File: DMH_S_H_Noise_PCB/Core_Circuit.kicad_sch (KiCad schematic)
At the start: 63 parts, among them Q1 BC548, Q2 MMBFJ113, Q3 BC548, SW1 SW_Push, SW2 SW_SPDT_321, U1 TL074, U2 TL072, U3 TL074

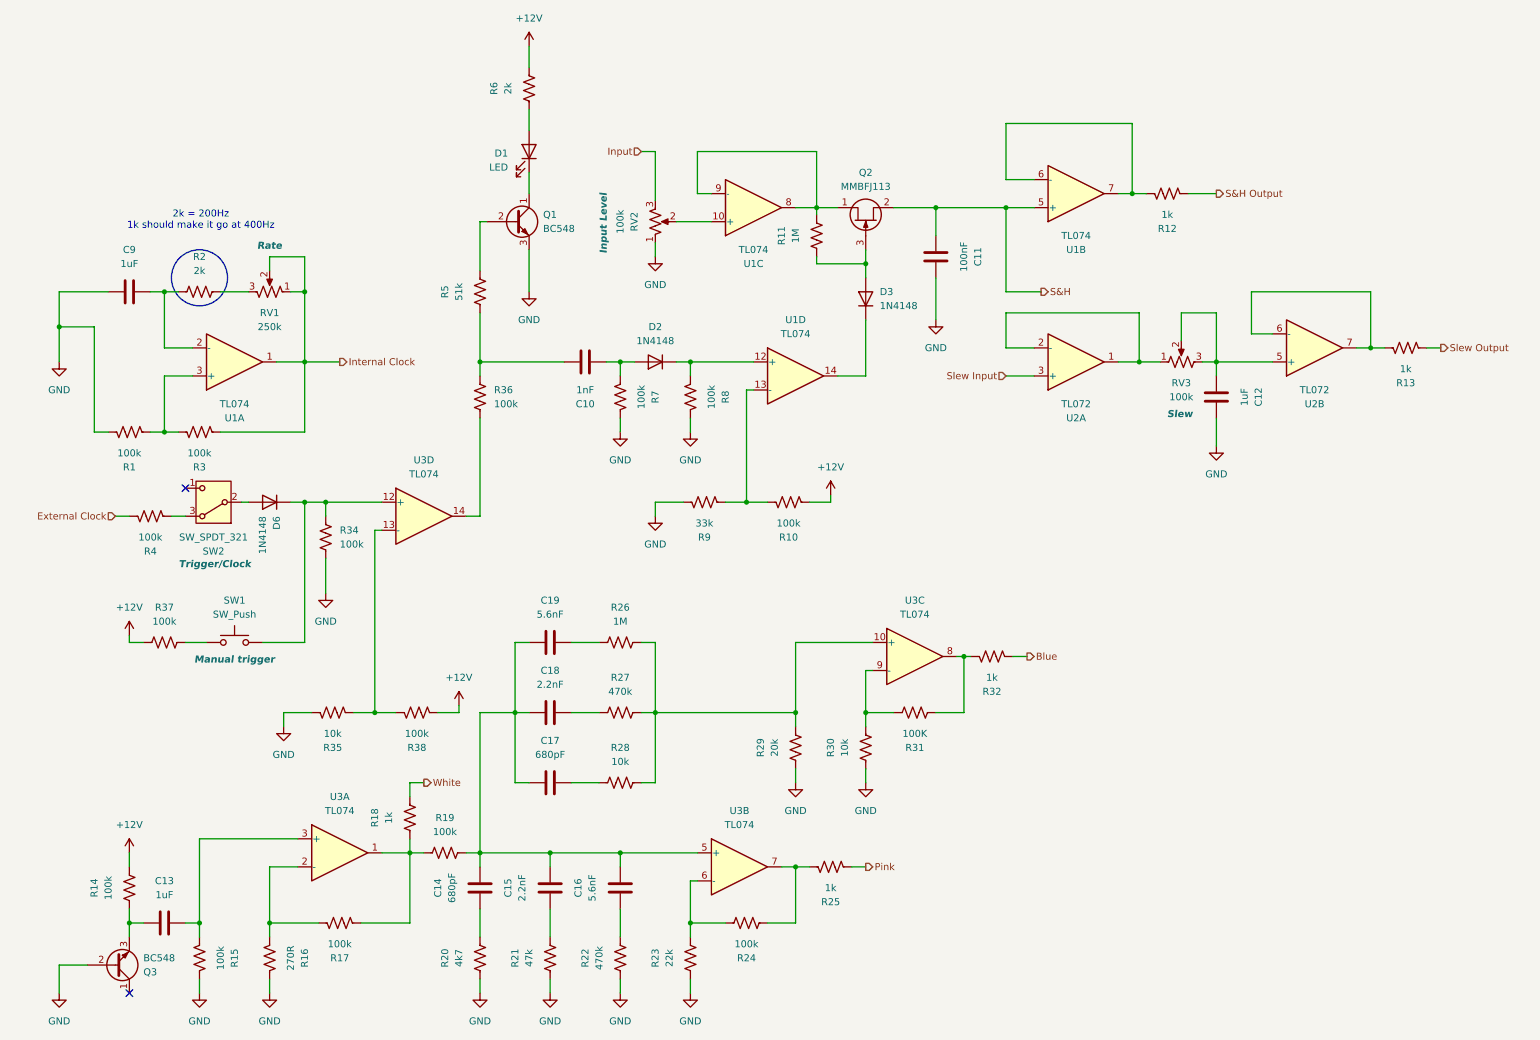
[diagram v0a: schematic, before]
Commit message: Added clock output
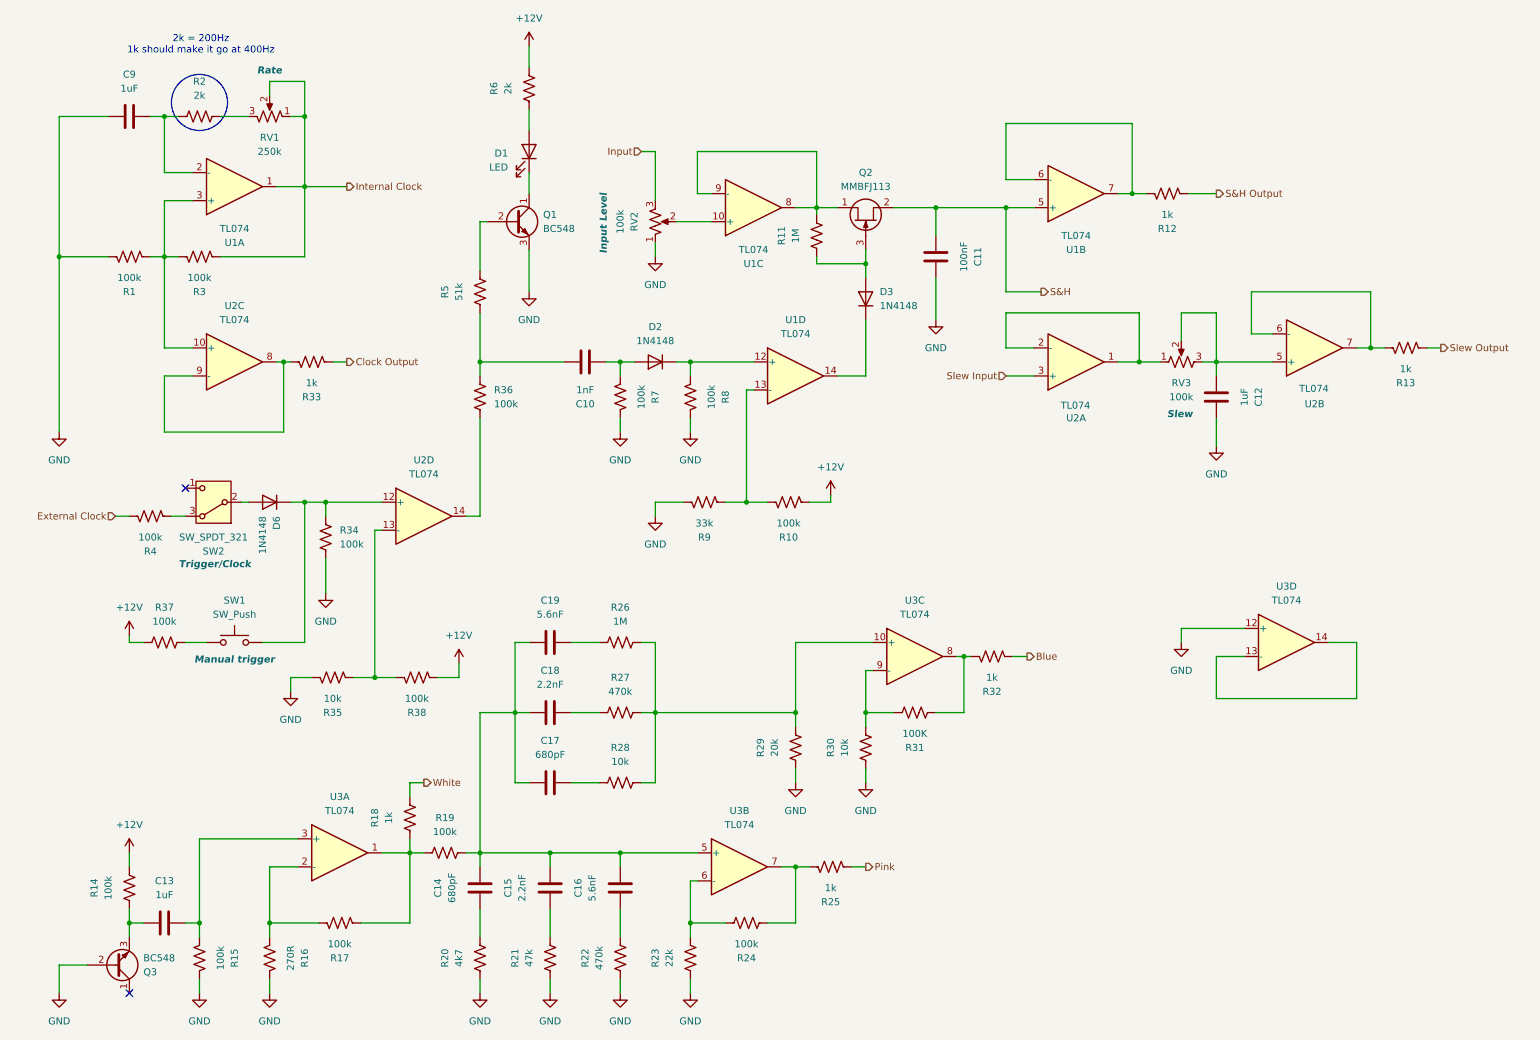
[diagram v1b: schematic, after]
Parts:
- added R33: 1k, Resistor_THT:R_Axial_DIN0207_L6.3mm_D2.5mm_P7.62mm_Horizontal, symbol Device:R_US
- added unit 3 of U2
- added unit 4 of U3
- SW1: footprint (none) -> Button_Switch_Keyboard:SW_Cherry_MX_1.00u_PCB
- SW2: footprint (none) -> SynthStuff:Toggle_Switch_THT
- U2: value TL072 -> TL074; footprint Package_DIP:DIP-8_W7.62mm_Socket -> Package_DIP:DIP-14_W7.62mm_Socket; symbol Amplifier_Operational:TL072 -> Amplifier_Operational:TL074
- renumbered U3 to U2
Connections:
- net GND: now also U3.12 (+)
- net at R1.1, R3.2, U1.3 (+): now also U2.10 (+)
- new net: R33.2, U2.8, U2.9 (-)
- new net: U3.13 (-), U3.14
- new net Clock Output: R33.1
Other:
- moved on the sheet: C9, R1, R2, R3, R35, R38, RV1, U1A

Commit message: Component placement ongoing
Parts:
- Q2: value MMBFJ113 -> J113; footprint Package_TO_SOT_SMD:SOT-23 -> Package_TO_SOT_THT:TO-92L_Inline
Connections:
- net at R4.1: now also SW2.1 (C); no longer SW2.3 (A)
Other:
- moved on the sheet: R4
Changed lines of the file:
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@@
 	)
 	(no_connect
-		(at 41.91 99.06)
+		(at 41.91 104.14)
 	)
 	(no_connect
@@
 	(wire
 		(pts
-			(xy 39.37 104.14) (xy 41.91 104.14)
-		)
-		(stroke
-			(width 0)
-			(type default)
-		)
-	)
-	(wire
-		(pts
 			(xy 101.6 127) (xy 101.6 139.7)
 		)
@@
 	(wire
 		(pts
-			(xy 29.21 104.14) (xy 31.75 104.14)
+			(xy 29.21 99.06) (xy 31.75 99.06)
 		)
 		(stroke
@@
 	(wire
 		(pts
+			(xy 39.37 99.06) (xy 41.91 99.06)
+		)
+		(stroke
+			(width 0)
+			(type default)
+		)
+	)
+	(wire
+		(pts
 			(xy 222.25 72.39) (xy 222.25 67.31)
 		)
@@
 	(hierarchical_label "External Clock"
 		(shape input)
-		(at 29.21 104.14 180)
+		(at 29.21 99.06 180)
 		(fields_autoplaced yes)
 		(effects
@@
 	(symbol
 		(lib_id "Device:R_US")
-		(at 35.56 104.14 270)
-		(mirror x)
+		(at 35.56 99.06 270)
 		(unit 1)
 		(exclude_from_sim no)
@@
 		(dnp no)
 		(property "Reference" "R4"
-			(at 35.56 110.49 90)
+			(at 35.56 92.71 90)
 			(effects
 				(font
@@
 		)
 		(property "Value" "100k"
-			(at 35.56 107.95 90)
+			(at 35.56 95.25 90)
 			(effects
 				(font
@@
 		)
 		(property "Footprint" "Resistor_THT:R_Axial_DIN0207_L6.3mm_D2.5mm_P7.62mm_Horizontal"
-			(at 35.306 103.124 90)
+			(at 35.306 100.076 90)
 			(effects
 				(font
@@
 		)
 		(property "Datasheet" "~"
-			(at 35.56 104.14 0)
+			(at 35.56 99.06 0)
 			(effects
 				(font
@@
 		)
 		(property "Description" "Resistor, US symbol"
-			(at 35.56 104.14 0)
+			(at 35.56 99.06 0)
 			(effects
 				(font
@@
 			)
 		)
-		(property "Value" "MMBFJ113"
+		(property "Value" "J113"
 			(at 165.1 44.45 90)
 			(effects
@@
 			)
 		)
-		(property "Footprint" "Package_TO_SOT_SMD:SOT-23"
+		(property "Footprint" "Package_TO_SOT_THT:TO-92L_Inline"
 			(at 167.005 45.72 0)
 			(effects
@@
 			)
 		)
+		(property "Function" ""
+			(at 165.1 50.8 0)
+			(effects
+				(font
+					(size 1.27 1.27)
+				)
+			)
+		)

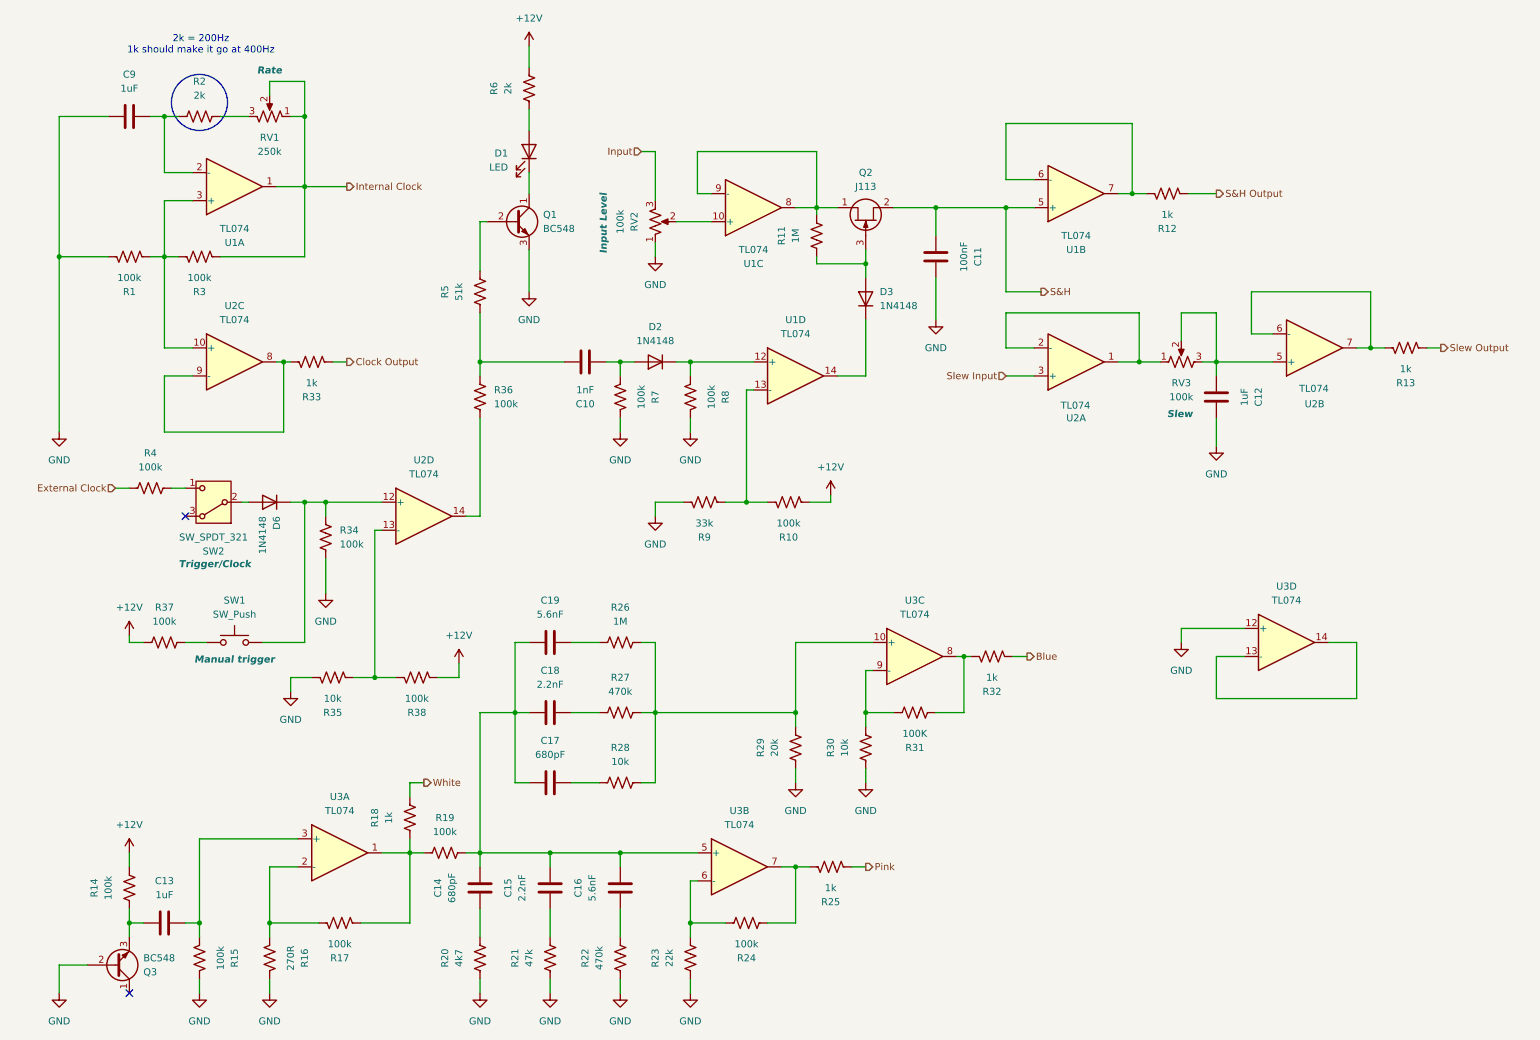
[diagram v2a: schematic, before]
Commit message: Restarted positioning from scratch
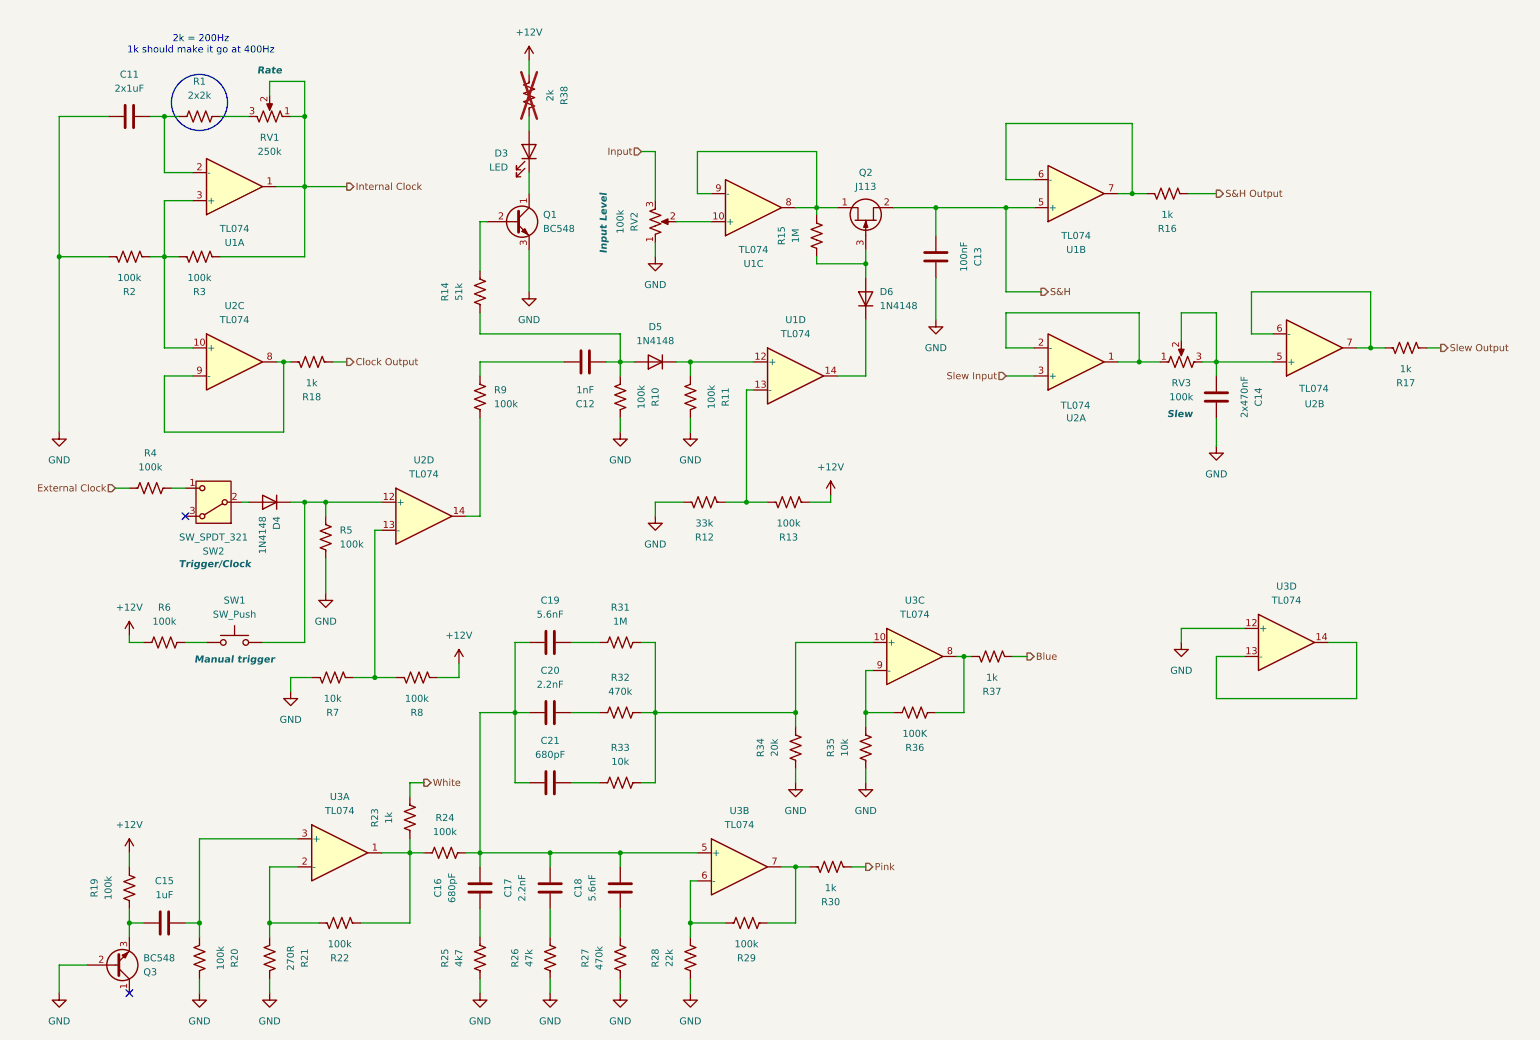
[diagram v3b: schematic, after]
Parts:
- removed R6: 2k, Resistor_THT:R_Axial_DIN0207_L6.3mm_D2.5mm_P7.62mm_Horizontal, symbol Device:R_US
- added R38: 2k, Resistor_THT:R_Axial_DIN0207_L6.3mm_D2.5mm_P7.62mm_Horizontal, symbol Device:R_US
- C11: renamed from C9; value 1uF -> 2x1uF
- C14: renamed from C12; value 1uF -> 2x470nF
- R1: renamed from R2; value 2k -> 2x2k
- renumbered C10 to C12, C11 to C13, C13 to C15, C14 to C16, C15 to C17, C16 to C18, C18 to C20, C17 to C21, D1 to D3, D6 to D4, D2 to D5, D3 to D6, R7 to R10, R8 to R11, R9 to R12, R10 to R13, R5 to R14, R11 to R15, R12 to R16, R13 to R17, R33 to R18, R14 to R19, R1 to R2, R15 to R20, R16 to R21, R17 to R22, R18 to R23, R19 to R24, R20 to R25, R21 to R26, R22 to R27, R23 to R28, R24 to R29, R25 to R30, R26 to R31, R27 to R32, R28 to R33, R29 to R34, R30 to R35, R31 to R36, R32 to R37, R34 to R5, R37 to R6, R35 to R7, R38 to R8, R36 to R9
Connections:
- net +12V: now also R38.1
- net at D3.2 (A): now also R38.2
- net at C12.2, R9.2: no longer R14.2
- net at C12.1, D5.2 (A), R10.1: now also R14.2

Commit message: Minor positioning corrections
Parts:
- RV1, RV2, RV3: footprint Potentiometer_THT:Potentiometer_Alpha_RD901F-40-00D_Single_Vertical -> SynthStuff:Potentiometer_Alpha_RD901F-40-00D_Single_Vertical
- SW1: footprint Button_Switch_Keyboard:SW_Cherry_MX_1.00u_PCB -> SynthStuff:SW_Cherry_MX_1.00u_PCB
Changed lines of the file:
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@@
 			)
 		)
-		(property "Footprint" "Potentiometer_THT:Potentiometer_Alpha_RD901F-40-00D_Single_Vertical"
+		(property "Footprint" "SynthStuff:Potentiometer_Alpha_RD901F-40-00D_Single_Vertical"
 			(at 222.25 76.2 0)
 			(effects
@@
 			)
 		)
-		(property "Footprint" "Potentiometer_THT:Potentiometer_Alpha_RD901F-40-00D_Single_Vertical"
+		(property "Footprint" "SynthStuff:Potentiometer_Alpha_RD901F-40-00D_Single_Vertical"
 			(at 127 50.8 0)
 			(effects
@@
 			)
 		)
-		(property "Footprint" "Potentiometer_THT:Potentiometer_Alpha_RD901F-40-00D_Single_Vertical"
+		(property "Footprint" "SynthStuff:Potentiometer_Alpha_RD901F-40-00D_Single_Vertical"
 			(at 57.15 31.75 0)
 			(effects
@@
 			)
 		)
-		(property "Footprint" "Button_Switch_Keyboard:SW_Cherry_MX_1.00u_PCB"
+		(property "Footprint" "SynthStuff:SW_Cherry_MX_1.00u_PCB"
 			(at 50.8 121.92 0)
 			(effects

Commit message: Minor corrections
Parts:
- R38: value 2k -> 100R; now fitted
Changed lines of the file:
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@@
 		(in_bom yes)
 		(on_board yes)
-		(dnp yes)
+		(dnp no)
 		(property "Reference" "R38"
 			(at 110.49 27.94 90)
@@
 			)
 		)
-		(property "Value" "2k"
+		(property "Value" "100R"
 			(at 107.95 27.94 90)
 			(effects
